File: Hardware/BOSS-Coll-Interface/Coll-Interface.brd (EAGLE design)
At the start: 88.9 x 38.1 mm, 5 parts, among them J1 Amphenol 75869-330LF, J2 TE_1-2834016-2, X1 TE 5747835-4

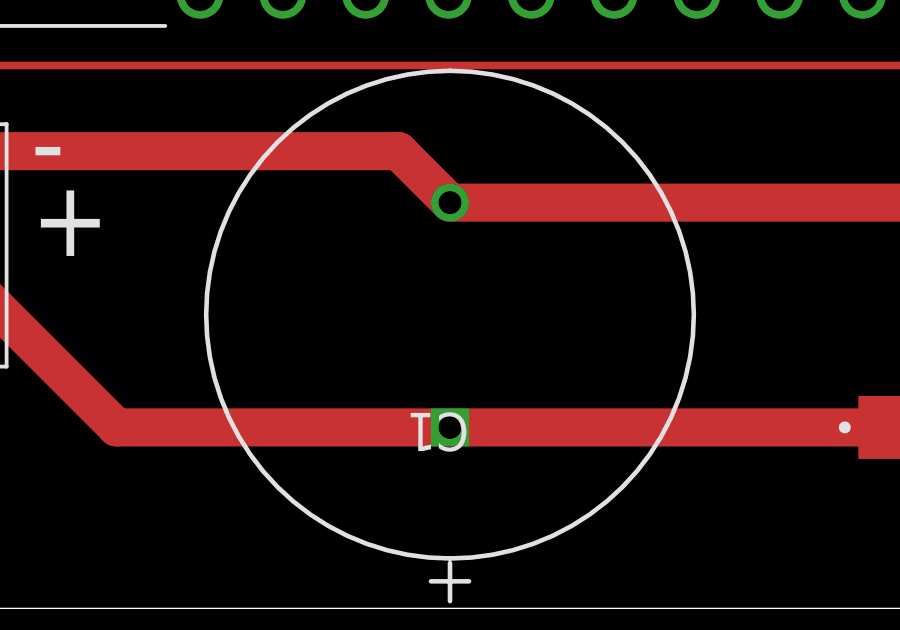
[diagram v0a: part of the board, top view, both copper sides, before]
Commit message: Changed hole size on capacitor leads
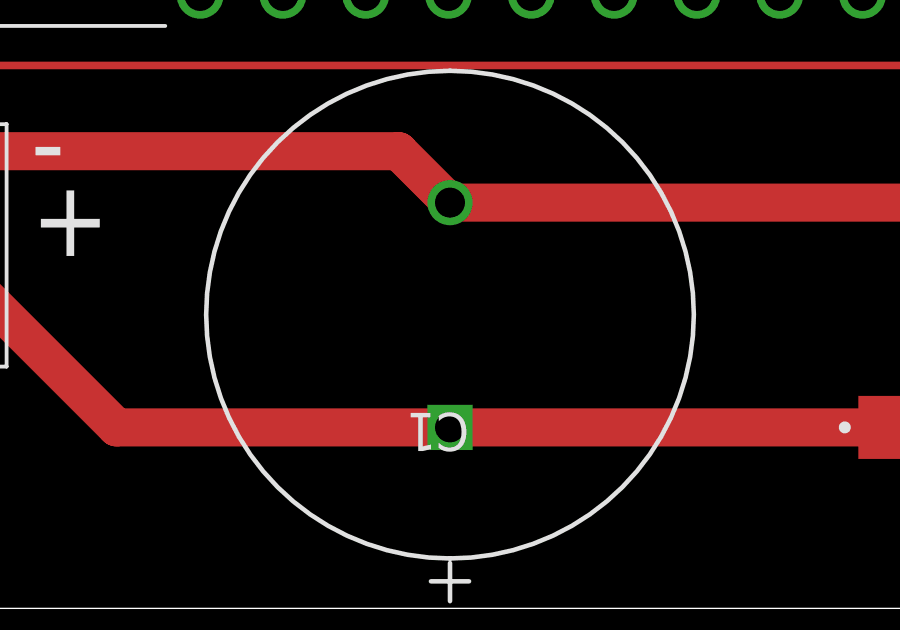
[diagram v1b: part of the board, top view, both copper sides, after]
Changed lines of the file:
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@@
 </autorouter>
 <elements>
-<element name="C1" library="AUmlib" library_urn="urn:adsk.eagle:library:9166017" package="U1-EE_NCH" package3d_urn="urn:adsk.eagle:package:27672260/2" value="UHE1H471MHD3" x="29.21" y="6.0325" smashed="yes" rot="R90">
+<element name="C1" library="AUmlib" library_urn="urn:adsk.eagle:library:9166017" package="U1-EE_NCH" package3d_urn="urn:adsk.eagle:package:27672260/3" value="UHE1H471MHD3" x="29.21" y="6.0325" smashed="yes" rot="R90">
 <attribute name="BUILT_BY" value="EMA_UL_Team" x="66.04" y="70.8025" size="1.778" layer="27" rot="R90" display="off"/>
 <attribute name="MANUFACTURER_PART_NUMBER" value="UHE1H471MHD3" x="66.04" y="70.8025" size="1.778" layer="27" rot="R90" display="off"/>
